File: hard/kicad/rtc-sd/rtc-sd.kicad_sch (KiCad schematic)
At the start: 39 parts, among them J1 SIDECAR, J2 SD0, J3 SD1, J4 SPI2, J5 SPI3, J6 RTC, J7 EXPANSION, Q1 2N7000, U1 74HC138, U2 74HC174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

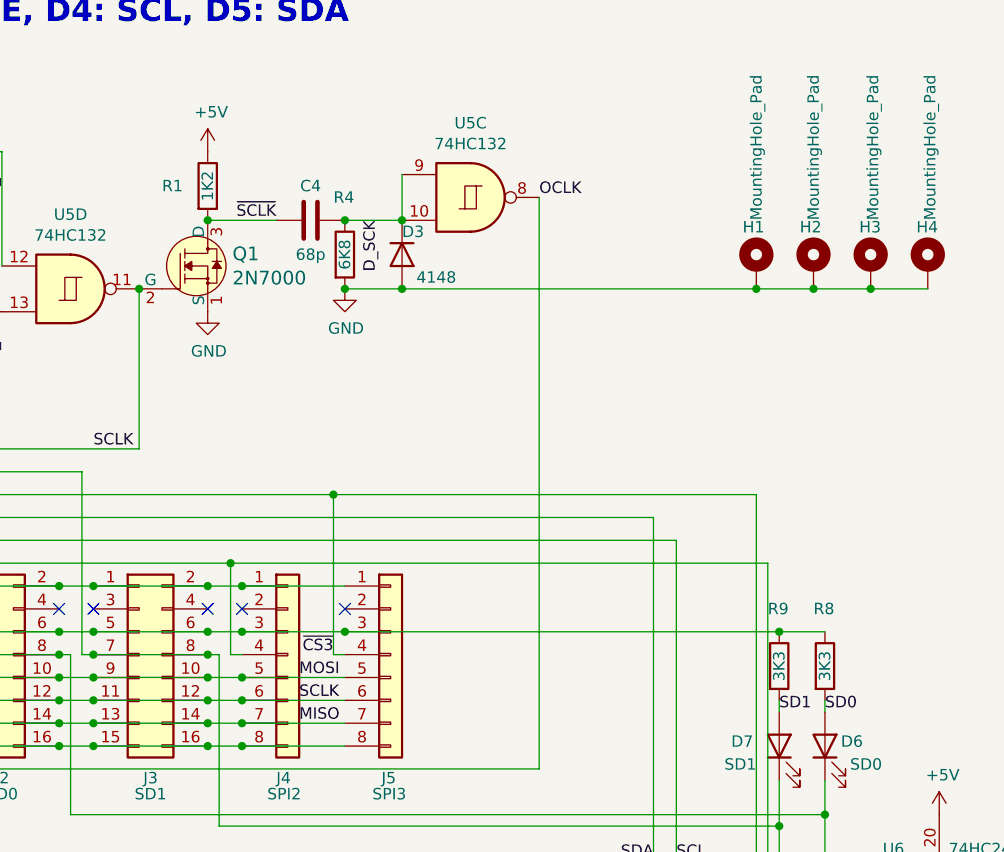
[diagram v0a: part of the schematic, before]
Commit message: minor passive repositioning
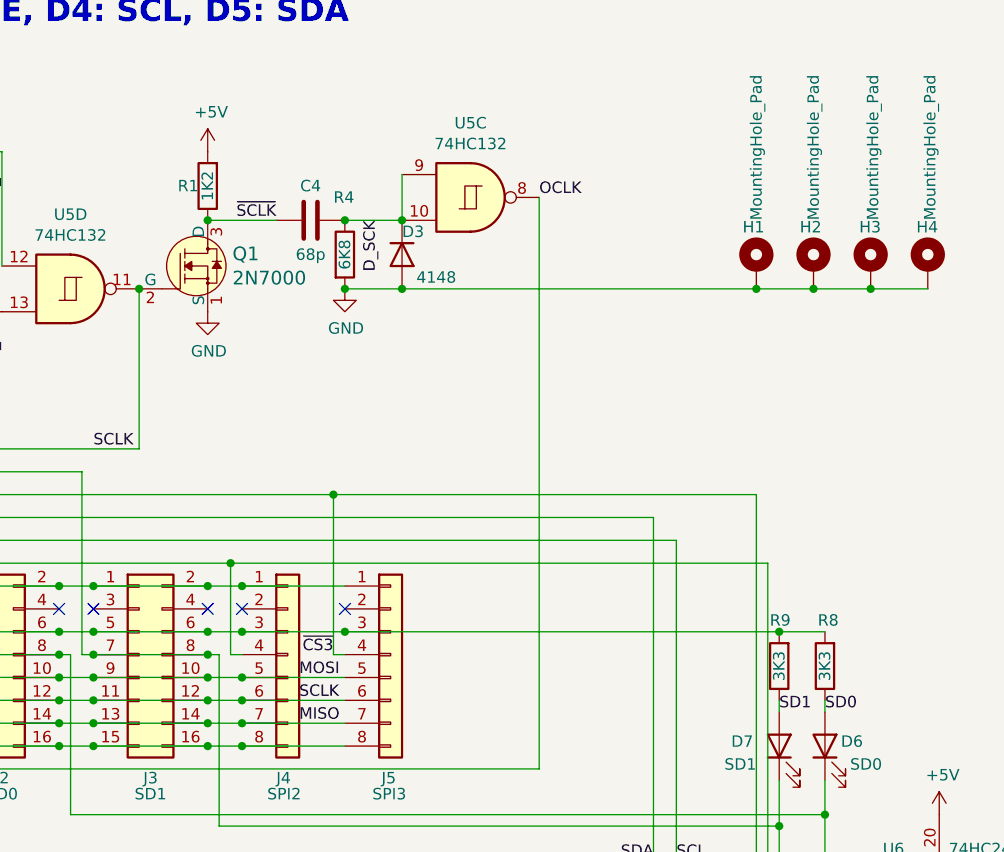
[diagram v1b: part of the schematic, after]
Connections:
- net +5V: now also R1.2, R8.2, R9.2; no longer R1.1, R8.1, R9.1
- net SD0: now also R8.1; no longer R8.2
- net SD1: now also R9.1; no longer R9.2
- net ~{SCLK}: now also R1.1; no longer R1.2
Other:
- moved on the sheet: R1, R8, R9
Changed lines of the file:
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@@
 	)
 	(junction
+		(at 243.84 99.06)
+		(diameter 0)
+		(color 0 0 0 0)
+	)
+	(junction
 		(at 184.15 99.06)
 		(diameter 0)
@@
 	)
 	(junction
-		(at 243.84 99.06)
-		(diameter 0)
-		(color 0 0 0 0)
-	)
-	(junction
 		(at 254 60.96)
 		(diameter 0)
@@
 	)
 	(junction
-		(at 180.34 53.34)
-		(diameter 0)
-		(color 0 0 0 0)
-	)
-	(junction
 		(at 102.87 118.11)
 		(diameter 0)
@@
 	)
 	(junction
+		(at 180.34 53.34)
+		(diameter 0)
+		(color 0 0 0 0)
+	)
+	(junction
 		(at 163.83 104.14)
 		(diameter 0)
@@
 	(wire
 		(pts
-			(xy 243.84 99.06) (xy 248.92 99.06)
-		)
-		(stroke
-			(width 0)
-			(type default)
-		)
-	)
-	(wire
-		(pts
 			(xy 102.87 118.11) (xy 102.87 125.73)
 		)
@@
 	(wire
 		(pts
+			(xy 243.84 99.06) (xy 248.92 99.06)
+		)
+		(stroke
+			(width 0)
+			(type default)
+		)
+	)
+	(wire
+		(pts
 			(xy 195.58 53.34) (xy 201.93 53.34)
 		)
@@
 	(symbol
 		(lib_id "Device:R")
-		(at 180.34 49.53 0)
+		(at 180.34 49.53 180)
 		(unit 1)
 		(exclude_from_sim no)
@@
 		(dnp no)
 		(property "Reference" "R1"
-			(at 175.26 49.53 0)
+			(at 179.324 49.53 0)
 			(effects
 				(font
@@
 		)
 		(property "Footprint" "Resistor_THT:R_Axial_DIN0207_L6.3mm_D2.5mm_P2.54mm_Vertical"
-			(at 178.562 49.53 90)
+			(at 182.118 49.53 90)
 			(effects
 				(font
@@
 	(symbol
 		(lib_id "Device:R")
-		(at 243.84 102.87 0)
+		(at 243.84 102.87 180)
 		(unit 1)
 		(exclude_from_sim no)
@@
 		(dnp no)
 		(property "Reference" "R9"
-			(at 242.57 96.52 0)
+			(at 245.11 97.79 0)
 			(effects
 				(font
@@
 		)
 		(property "Footprint" "Resistor_THT:R_Axial_DIN0207_L6.3mm_D2.5mm_P2.54mm_Vertical"
-			(at 242.062 102.87 90)
+			(at 245.618 102.87 90)
 			(effects
 				(font
@@
 	(symbol
 		(lib_id "Device:R")
-		(at 248.92 102.87 0)
+		(at 248.92 102.87 180)
 		(unit 1)
 		(exclude_from_sim no)
@@
 		(dnp no)
 		(property "Reference" "R8"
-			(at 247.65 96.52 0)
+			(at 250.444 97.79 0)
 			(effects
 				(font
@@
 		)
 		(property "Footprint" "Resistor_THT:R_Axial_DIN0207_L6.3mm_D2.5mm_P2.54mm_Vertical"
-			(at 247.142 102.87 90)
+			(at 250.698 102.87 90)
 			(effects
 				(font

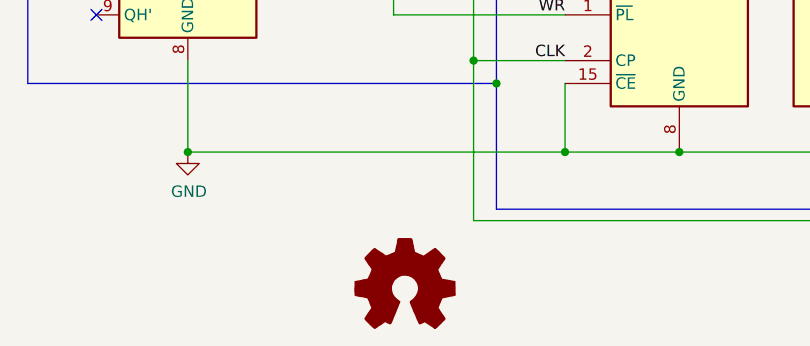
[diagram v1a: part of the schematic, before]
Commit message: add dron author and J-logo to RTC-SD
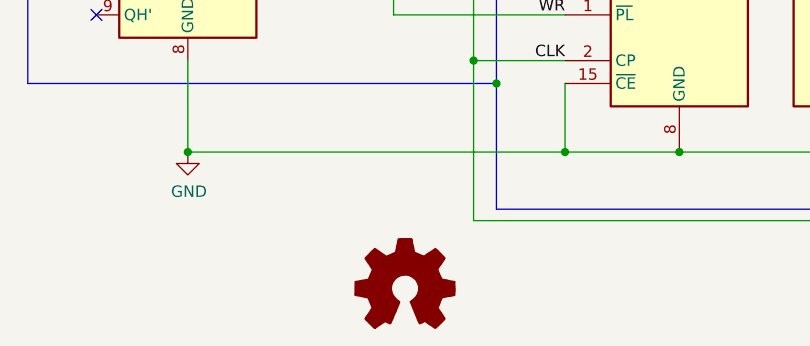
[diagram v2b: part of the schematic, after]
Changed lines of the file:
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@@
 		(lib_id "Graphic:Logo_Open_Hardware_Small")
 		(at 85.09 181.61 0)
+		(mirror y)
 		(unit 1)
 		(exclude_from_sim no)
